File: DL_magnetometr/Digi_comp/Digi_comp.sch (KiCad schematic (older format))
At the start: 51 parts, among them J1 USB_B_Micro, J2 Conn_01x06_Male, U1 NUP2202, U2 AZ4558CM, U3 AZ4558CM, U4 74AHCT1G125, U5 AP7331-WG-7, U6 HC-06, U7 JST-PHR-2, U8 AP7331-WG-7, U9 ATmega328P-MU

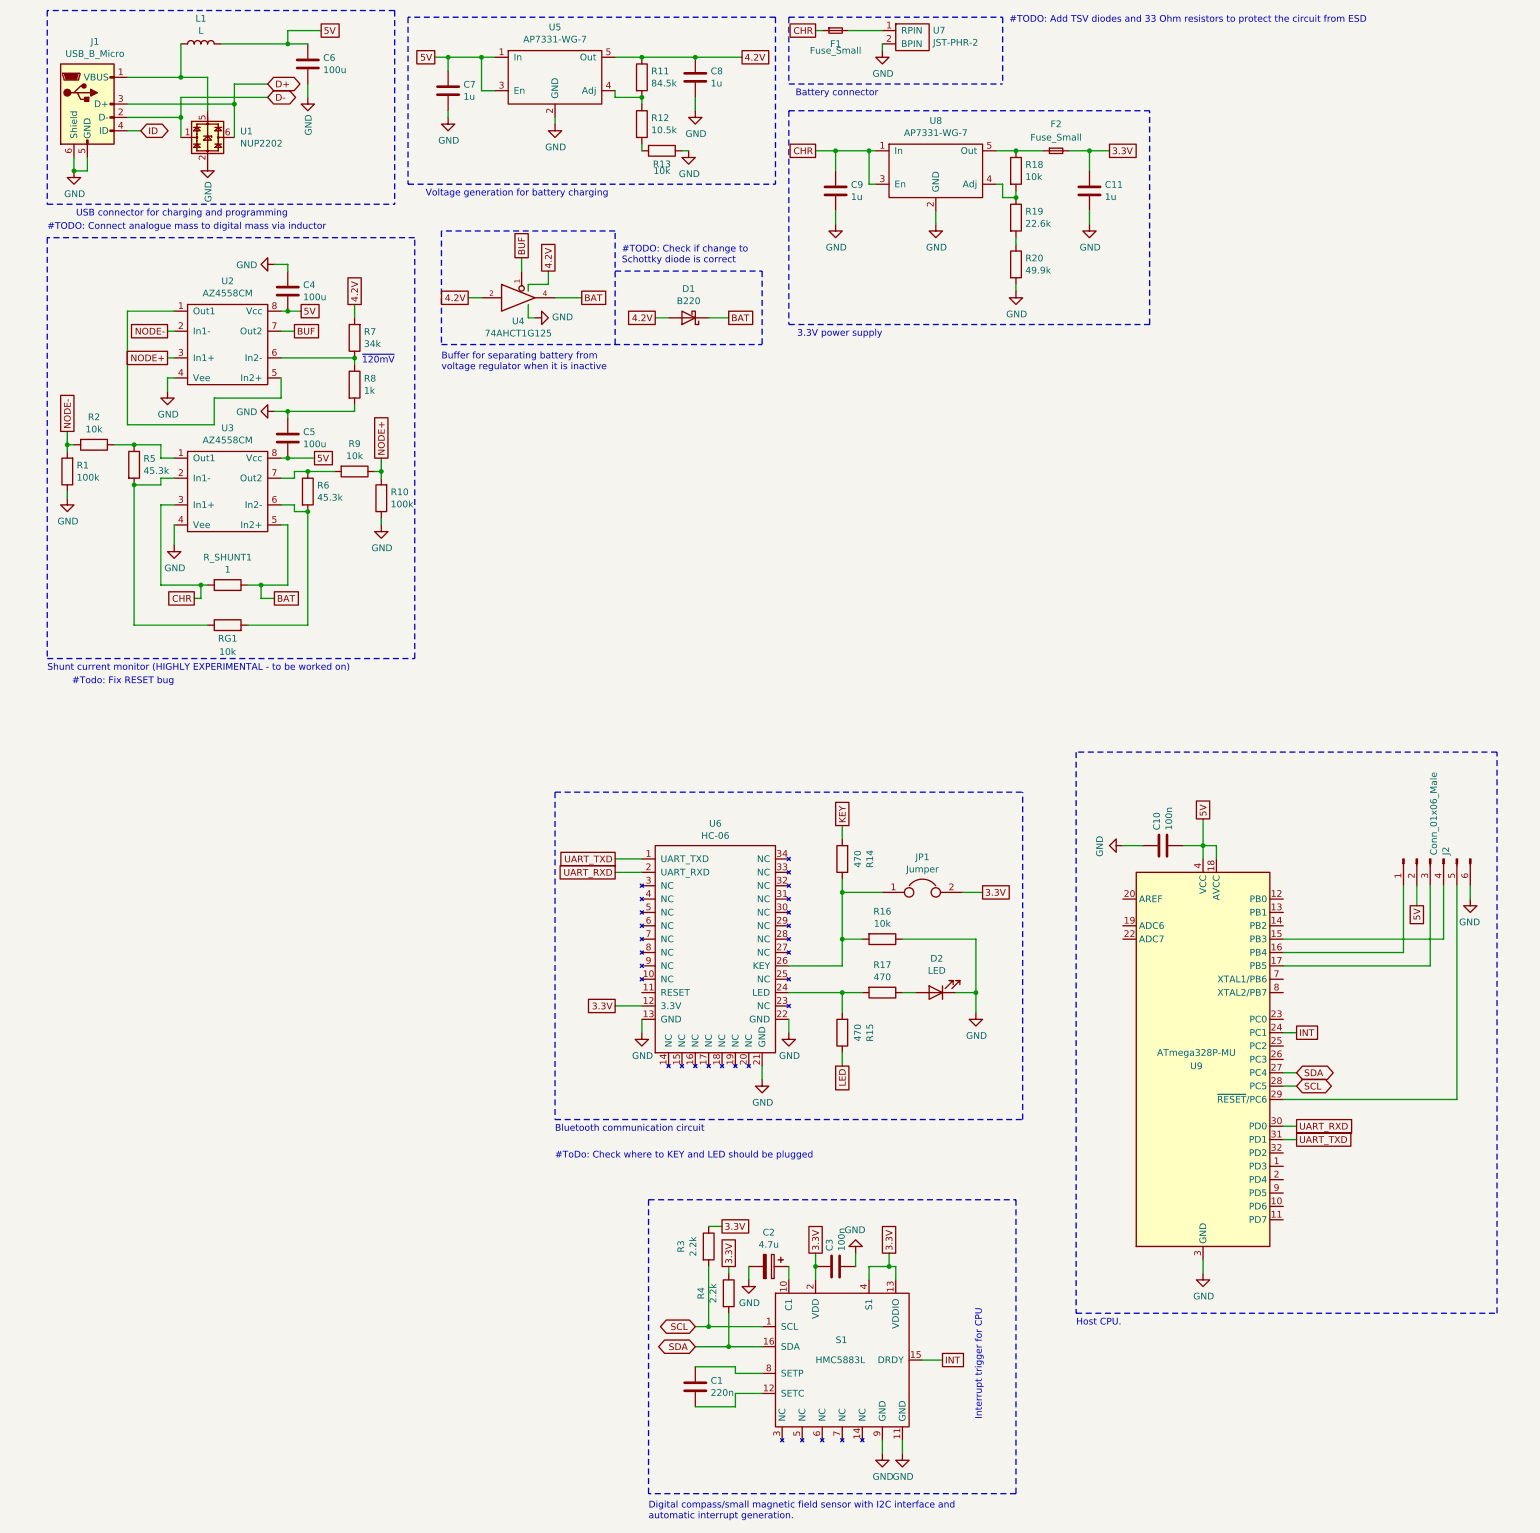
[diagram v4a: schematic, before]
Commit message: Changed power supply to battery.
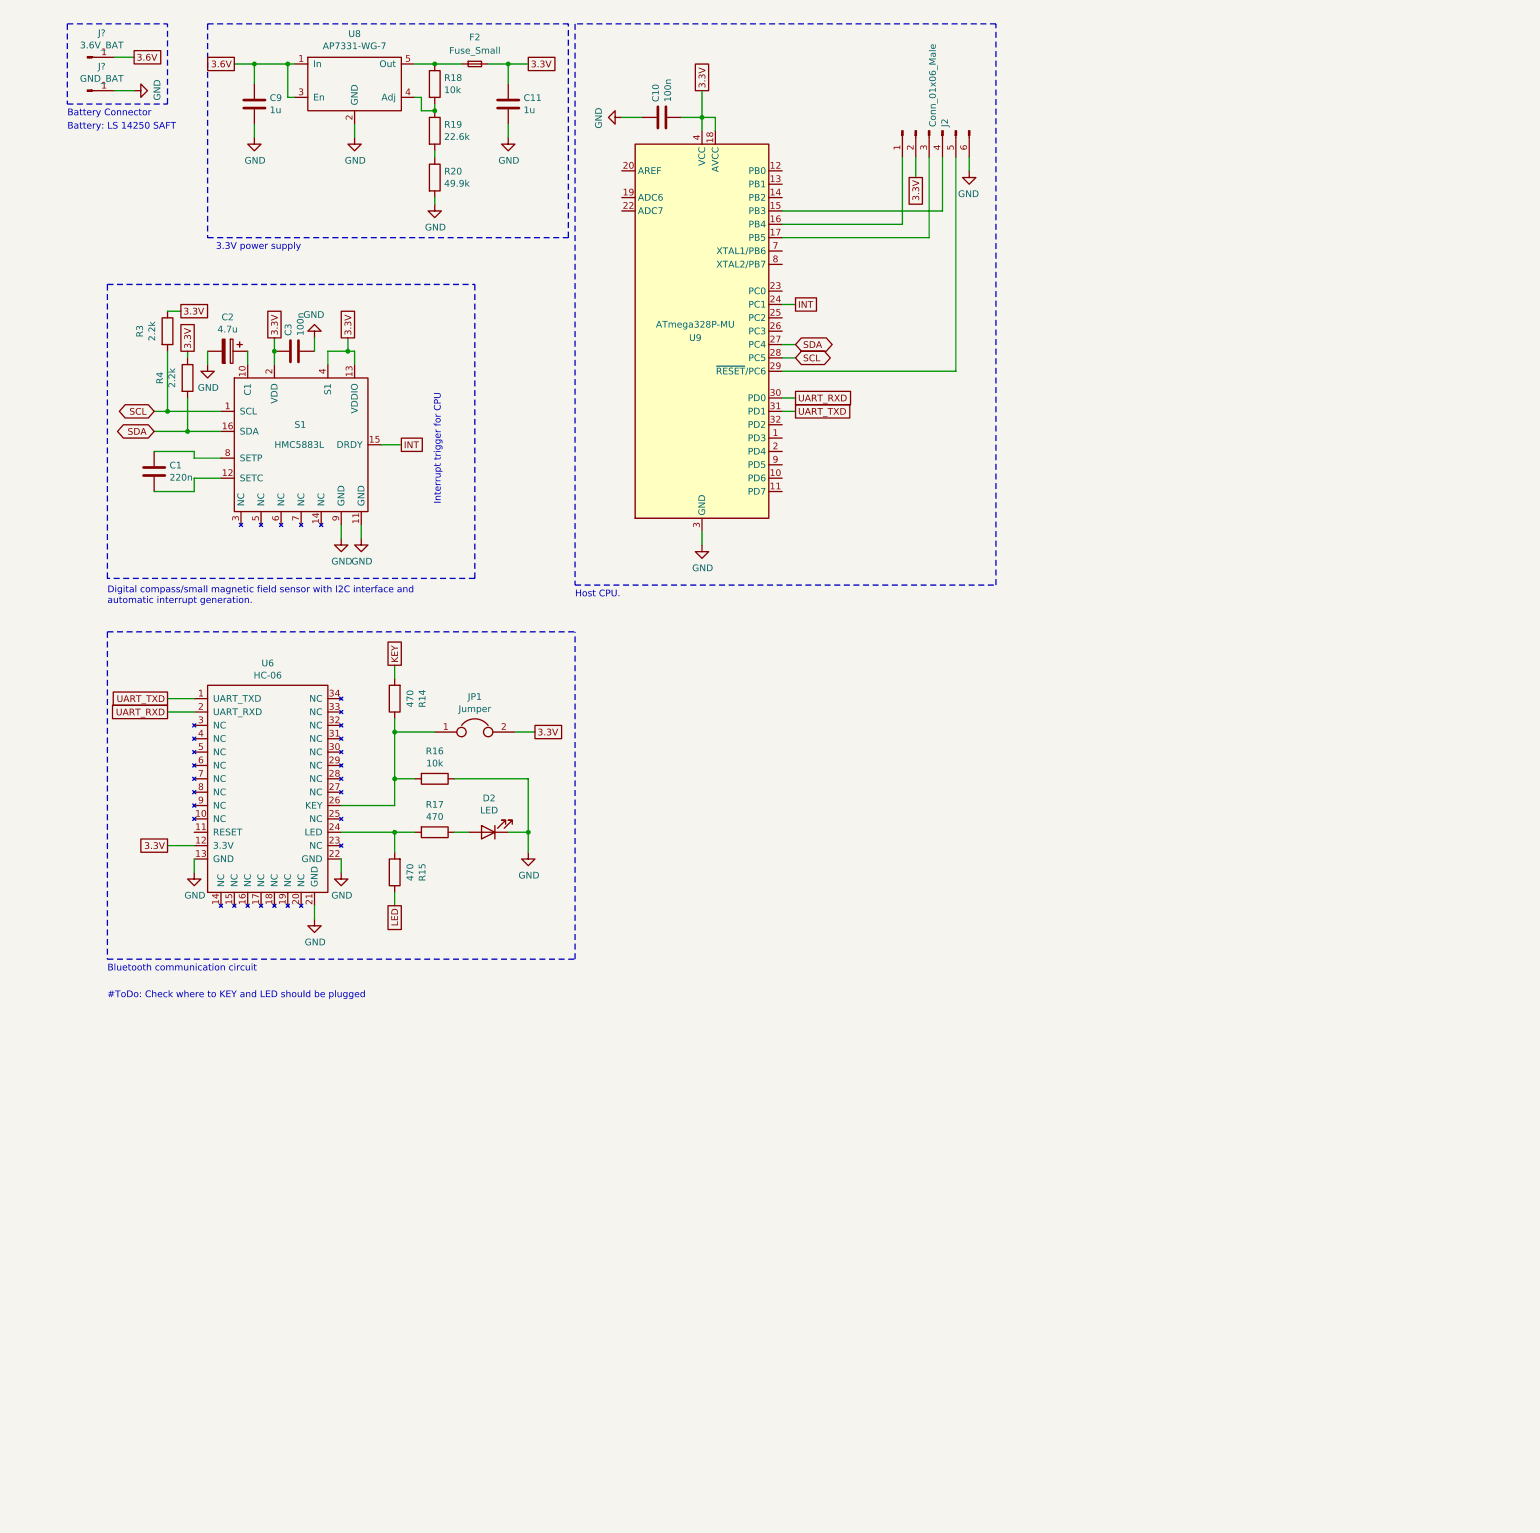
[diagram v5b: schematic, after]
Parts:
- removed C4, C5, C6: 100u, symbol Device:C
- removed C7, C8: 1u, symbol Device:C
- removed D1: B220, Diode_SMD:D_SMB, symbol Diode:B220
- removed F1: Fuse_Small, symbol Device:Fuse_Small
- removed J1: USB_B_Micro, symbol Connector:USB_B_Micro
- removed L1: L, symbol Device:L
- removed R1, R10: 100k, symbol Device:R
- removed R11: 84.5k, symbol Device:R
- removed R12: 10.5k, symbol Device:R
- removed R13, R2, R9, RG1: 10k, symbol Device:R
- removed R5, R6: 45.3k, symbol Device:R
- removed R7: 34k, symbol Device:R
- removed R8: 1k, symbol Device:R
- removed R_SHUNT1: 1, symbol Device:R
- removed U1: NUP2202, Package_TO_SOT_SMD:SOT-363_SC-70-6, symbol Power_Protection:NUP2202
- removed U2, U3: AZ4558CM, symbol Digi_comp-rescue:AZ4558CM-Amplifier_Audio
- removed U4: 74AHCT1G125, symbol 74xGxx:74AHCT1G125
- removed U5: AP7331-WG-7, Package_TO_SOT_SMD:TSOT-23-5, symbol Digi_comp-rescue:AP7331-WG-7-Regulator_Linear
- removed U7: JST-PHR-2, symbol Digi_comp-rescue:JST-PHR-2-Connector
- added J?: 3.6V_BAT, symbol Connector:Conn_01x01_Male
- added J?: GND_BAT, symbol Connector:Conn_01x01_Male
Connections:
- net 5V is gone; now on net 3.3V: C10.1, J2.2 (Pin_2), U9.18 (AVCC), U9.4 (VCC), U9.6 (VCC)
- net GND: now also J?.1 (Pin_1)
- net CHR renamed 3.6V
- net 3.6V: now also J?.1 (Pin_1)
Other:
- note added: "Battery Connector"
- note added: "Battery: LS 14250 SAFT"
- note removed: "#TODO: Add TSV diodes and 33 Ohm resistors to protect the circuit from ESD"
- note removed: "#TODO: Check if change to \nSchottky diode is correct\n"
- note removed: "#TODO: Connect analogue mass to digital mass via inductor"
- note removed: "#Todo: Fix RESET bug\n"
- note removed: "Battery connector"
- note removed: "Buffer for separating battery from \nvoltage regulator when it is inactive"
- note removed: "Shunt current monitor (HIGHLY EXPERIMENTAL - to be worked on)"
- note removed: "USB connector for charging and programming"
- note removed: "Voltage generation for battery charging"
- note removed: "~120mV"
- moved on the sheet: C1, C10, C11, C2, C3, C9, D2, F2, J2, JP1, R14, R15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

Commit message: Layout continuation
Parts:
- removed J?: 3.6V_BAT, symbol Connector:Conn_01x01_Male
- removed J?: GND_BAT, symbol Connector:Conn_01x01_Male
- added U1: JST-PHR-2-Connector, Dokumenty:2AA-SM, symbol Digi_comp-rescue:JST-PHR-2-Connector
- C4: renamed from C9; footprint (none) -> Capacitor_SMD:C_0805_2012Metric
- C5: renamed from C11; footprint (none) -> Capacitor_SMD:C_0805_2012Metric
- F1: renamed from F2; footprint (none) -> Fuse:Fuse_0805_2012Metric
- JP1: footprint Jumper:SolderJumper-3_P1.3mm_Bridged12_Pad1.0x1.5mm -> Jumper:SolderJumper-2_P1.3mm_Open_Pad1.0x1.5mm
- renumbered C10 to C6, D2 to D1, J2 to J1, R3 to R1, R4 to R2, R14 to R3, R15 to R4, R16 to R5, R17 to R6, R18 to R7, R19 to R8, R20 to R9, U6 to U2, U8 to U3, U9 to U4
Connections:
- net 3.6V: now also U1.1 (RPIN)
- net GND: now also U1.2 (BPIN)
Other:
- moved on the sheet: C4, C5, C6, F1, J1, R7, R8, R9, U3, U4

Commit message: Layout finished
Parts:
- removed U1: JST-PHR-2-Connector, Dokumenty:2AA-SM, symbol Digi_comp-rescue:JST-PHR-2-Connector
- added BT1: Battery_Cell, Dokumenty:2AA-SM, symbol Device:Battery_Cell
- added J2, J3: Conn_01x01_Male, Connector_PinHeader_2.54mm:PinHeader_1x01_P2.54mm_Vertical, symbol Connector:Conn_01x01_Male
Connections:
- net 3.6V: now also BT1.1 (+)
- net GND: now also BT1.2 (-)
- net KEY: no longer names the net of R3.2
- net KEY: now also J2.1 (Pin_1)
- net LED: no longer names the net of R4.1
- net LED: now also J3.1 (Pin_1)
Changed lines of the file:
@@
 	3100 6650 2700 6650
 Connection ~ 3100 6650
-Text GLabel 3100 7200 3    50   UnSpc ~ 0
-LED
-Wire Wire Line
-	3100 7200 3100 7100
 Wire Wire Line
 	2700 6450 3100 6450
@@
 	3400 5900 3100 5900
 Connection ~ 3100 5900
-Text GLabel 3100 5400 1    50   UnSpc ~ 0
-KEY
-Wire Wire Line
-	3100 5500 3100 5400
 Wire Wire Line
 	3650 6650 3550 6650
@@
 Text GLabel 6350 4900 2    50   BiDi ~ 0
 SDA
-Text GLabel 6350 5400 2    50   UnSpc ~ 0
-UART_TXD
 Wire Wire Line
 	6350 5400 6250 5400
-Text GLabel 6350 5300 2    50   UnSpc ~ 0
-UART_RXD
 Wire Wire Line
 	6350 5300 6250 5300
@@
 Wire Wire Line
 	3000 950  3250 950
-Connection ~ 3000 950
 Wire Wire Line
 	3000 1100 3000 950
-Wire Wire Line
-	2850 950  3000 950
 Wire Wire Line
 	4900 950  5050 950
@@
 Wire Notes Line
 	5300 2250 5300 650
-Wire Notes Line
-	2600 650  2600 2250
 Text GLabel 5050 950  2    50   UnSpc ~ 0
 3.3V
@@
 	1    0    0    -1
 $EndComp
-Text GLabel 2850 950  0    50   UnSpc ~ 0
-3.6V
 Text GLabel 5650 3000 1    50   UnSpc ~ 0
 3.3V
 Text GLabel 7250 3650 3    50   UnSpc ~ 0
 3.3V
-Wire Notes Line
-	650  600  650  1200
 Text Notes 650  1300 0    50   ~ 0
 Battery Connector
 Text Notes 650  1400 0    50   ~ 0
 Battery: LS 14250 SAFT
+Text Notes 950  7900 0    50   ~ 0
+#ToDo: Check where to KEY and LED should be plugged\n
+Wire Notes Line
+	1650 600  1650 1200
+Text GLabel 6350 5400 2    50   UnSpc ~ 0
+UART_TXD
+Text GLabel 6350 5300 2    50   UnSpc ~ 0
+UART_RXD
+Wire Wire Line
+	1000 750  900  750
 Text GLabel 900  750  0    50   UnSpc ~ 0
 3.6V
@@
 L power:GND #PWR01
 U 1 1 601C4065
-P 900 850
-F 0 "#PWR01" H 900 600 50  0001 C CNN
-F 1 "GND" H 905 677 50  0000 C CNN
-F 2 "" H 900 850 50  0001 C CNN
-F 3 "" H 900 850 50  0001 C CNN
-	1    900  850
-	1    0    0    -1
-$EndComp
-Text Notes 950  7900 0    50   ~ 0
-#ToDo: Check where to KEY and LED should be plugged\n
-$Comp
-L Digi_comp-rescue:JST-PHR-2-Connector U1
-U 1 1 600EB782
-P 1200 550
-F 0 "U1" H 1378 351 50  0000 L CNN
-F 1 "JST-PHR-2-Connector" H 1378 260 50  0000 L CNN
-F 2 "Dokumenty:2AA-SM" H 1200 550 50  0001 C CNN
-F 3 "" H 1200 550 50  0001 C CNN
-	1    1200 550
-	1    0    0    -1
-$EndComp
-Wire Wire Line
-	1000 750  900  750
-Wire Wire Line
-	1000 850  900  850
-Wire Notes Line
-	2300 600  2300 1200
-Wire Notes Line
-	2300 1200 650  1200
-Wire Notes Line
-	650  600  2300 600
+P 900 1050
+F 0 "#PWR01" H 900 800 50  0001 C CNN
+F 1 "GND" H 905 877 50  0000 C CNN
+F 2 "" H 900 1050 50  0001 C CNN
+F 3 "" H 900 1050 50  0001 C CNN
+	1    900  1050
+	0    1    1    0
+$EndComp
+$Comp
+L Device:Battery_Cell BT1
+U 1 1 60107D79
+P 1000 950
+F 0 "BT1" H 1118 1046 50  0000 L CNN
+F 1 "Battery_Cell" H 1118 955 50  0000 L CNN
+F 2 "Dokumenty:2AA-SM" V 1000 1010 50  0001 C CNN
+F 3 "~" V 1000 1010 50  0001 C CNN
+	1    1000 950
+	1    0    0    -1
+$EndComp
+Text GLabel 2850 950  0    50   UnSpc ~ 0
+3.6V
+Connection ~ 3000 950
+Wire Wire Line
+	2850 950  3000 950
+Wire Notes Line
+	2600 650  2600 2250
+Wire Wire Line
+	900  1050 1000 1050
+Wire Notes Line
+	1650 600  650  600
+Wire Notes Line
+	650  600  650  1200
+Wire Notes Line
+	1650 1200 650  1200
+$Comp
+L Connector:Conn_01x01_Male J3
+U 1 1 60155FF8
+P 2900 7400
+F 0 "J3" H 3008 7581 50  0000 C CNN
+F 1 "Conn_01x01_Male" H 3008 7490 50  0000 C CNN
+F 2 "Connector_PinHeader_2.54mm:PinHeader_1x01_P2.54mm_Vertical" H 2900 7400 50  0001 C CNN
+F 3 "~" H 2900 7400 50  0001 C CNN
+	1    2900 7400
+	1    0    0    -1
+$EndComp
+$Comp
+L Connector:Conn_01x01_Male J2
+U 1 1 60156BD7
+P 2900 5400
+F 0 "J2" H 3008 5581 50  0000 C CNN
+F 1 "Conn_01x01_Male" H 3008 5490 50  0000 C CNN
+F 2 "Connector_PinHeader_2.54mm:PinHeader_1x01_P2.54mm_Vertical" H 2900 5400 50  0001 C CNN
+F 3 "~" H 2900 5400 50  0001 C CNN
+	1    2900 5400
+	1    0    0    -1
+$EndComp
+Wire Wire Line
+	3100 7100 3100 7400
+Wire Wire Line
+	3100 5400 3100 5500
 $EndSCHEMATC

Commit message: Exit save
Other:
- note removed: "#ToDo: Check where to KEY and LED should be plugged\n"
- moved on the sheet: BT1
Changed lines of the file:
@@
 Text GLabel 7250 3650 3    50   UnSpc ~ 0
 3.3V
-Text Notes 650  1300 0    50   ~ 0
+Text Notes 1450 1800 0    50   ~ 0
 Battery Connector
-Text Notes 650  1400 0    50   ~ 0
+Text Notes 1450 1900 0    50   ~ 0
 Battery: LS 14250 SAFT
-Text Notes 950  7900 0    50   ~ 0
-#ToDo: Check where to KEY and LED should be plugged\n
 Wire Notes Line
-	1650 600  1650 1200
+	2450 1100 2450 1700
 Text GLabel 6350 5400 2    50   UnSpc ~ 0
 UART_TXD
@@
 UART_RXD
 Wire Wire Line
-	1000 750  900  750
-Text GLabel 900  750  0    50   UnSpc ~ 0
+	1800 1250 1700 1250
+Text GLabel 1700 1250 0    50   UnSpc ~ 0
 3.6V
 $Comp
 L power:GND #PWR01
 U 1 1 601C4065
-P 900 1050
-F 0 "#PWR01" H 900 800 50  0001 C CNN
-F 1 "GND" H 905 877 50  0000 C CNN
-F 2 "" H 900 1050 50  0001 C CNN
-F 3 "" H 900 1050 50  0001 C CNN
-	1    900  1050
+P 1700 1550
+F 0 "#PWR01" H 1700 1300 50  0001 C CNN
+F 1 "GND" H 1705 1377 50  0000 C CNN
+F 2 "" H 1700 1550 50  0001 C CNN
+F 3 "" H 1700 1550 50  0001 C CNN
+	1    1700 1550
 	0    1    1    0
 $EndComp
@@
 L Device:Battery_Cell BT1
 U 1 1 60107D79
-P 1000 950
-F 0 "BT1" H 1118 1046 50  0000 L CNN
-F 1 "Battery_Cell" H 1118 955 50  0000 L CNN
-F 2 "Dokumenty:2AA-SM" V 1000 1010 50  0001 C CNN
-F 3 "~" V 1000 1010 50  0001 C CNN
-	1    1000 950
+P 1800 1450
+F 0 "BT1" H 1918 1546 50  0000 L CNN
+F 1 "Battery_Cell" H 1918 1455 50  0000 L CNN
+F 2 "Dokumenty:2AA-SM" V 1800 1510 50  0001 C CNN
+F 3 "~" V 1800 1510 50  0001 C CNN
+	1    1800 1450
 	1    0    0    -1
 $EndComp
@@
 	2600 650  2600 2250
 Wire Wire Line
-	900  1050 1000 1050
+	1700 1550 1800 1550
 Wire Notes Line
-	1650 600  650  600
+	2450 1100 1450 1100
 Wire Notes Line
-	650  600  650  1200
+	1450 1100 1450 1700
 Wire Notes Line
-	1650 1200 650  1200
+	2450 1700 1450 1700
 $Comp
 L Connector:Conn_01x01_Male J3
